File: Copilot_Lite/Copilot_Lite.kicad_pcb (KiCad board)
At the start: 4 copper layers, 65 x 56 mm, 80 parts, among them J1 POWER_MODES, J11 SERIAL_MODE, J12 SERIAL_VOLTAGE_SELECT, J2 JACK_POWER_IN, J3 USB_POWER_IN, J4 USB_PC, J6 5V_ENABLE, J7 SERIAL_AND_GPIO, J8 JACK_POWER_OUT, J9 USB_POWER_OUT, Q1 BSS138, Q2 BUK7M27-80EX, Q3 BUK7M27-80EX, Q4 BSS138, Q5 BSS138, Q6 BSS138, Q7 BSS138, Q8 BSS138, Q9 BSS138, U1 LM74502, U2 LM74502, U3 AP2204K-ADJ, U4 AP2204K-ADJ, U5 FT230XS, U6 SN74LV1T125, U7 SN74LV1T125, U8 SN74LV1T125, U9 SN74LV1T125

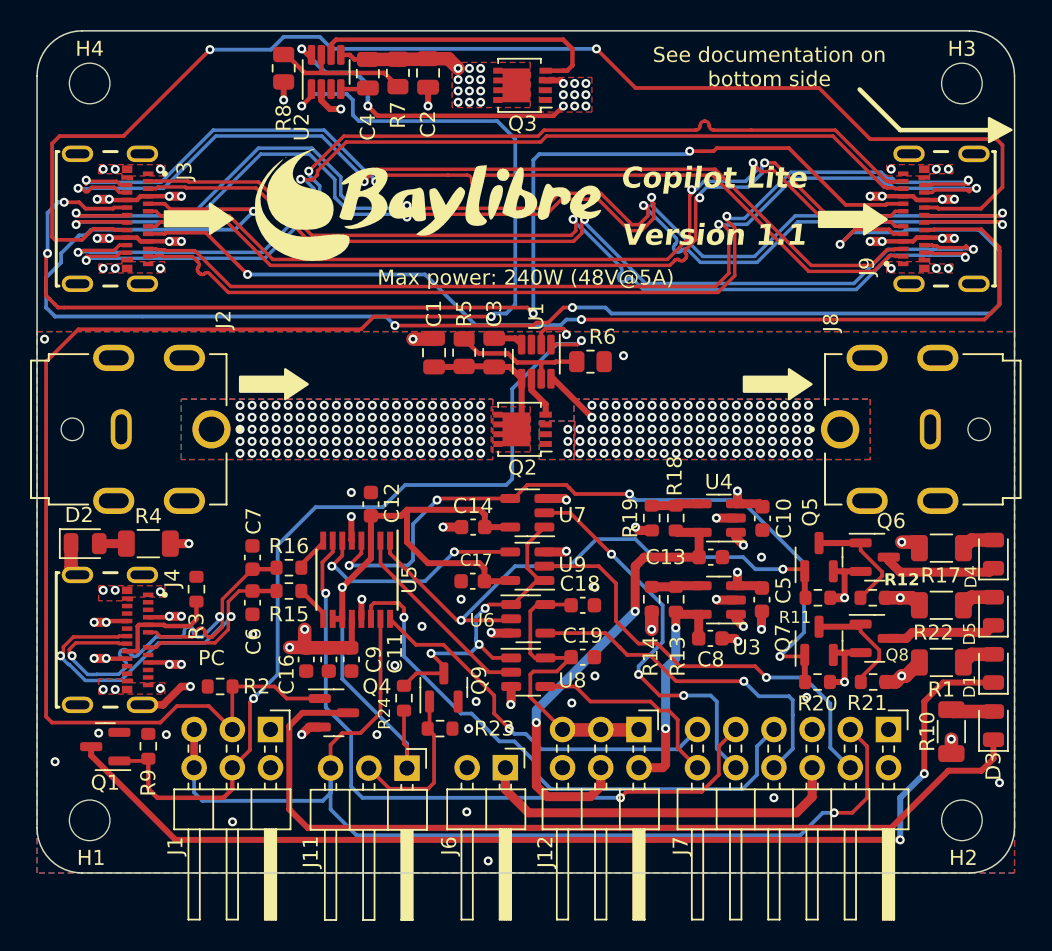
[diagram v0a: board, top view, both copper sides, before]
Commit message: lite: Added even more offset to the USB-C connector shield pins to further improve its centering.
The goal is to make sure all signal pads are well soldered even if the
connector is placed by a human.

Signed-off-by: Adrien Ricciardi <aricciardi@baylibre.com>
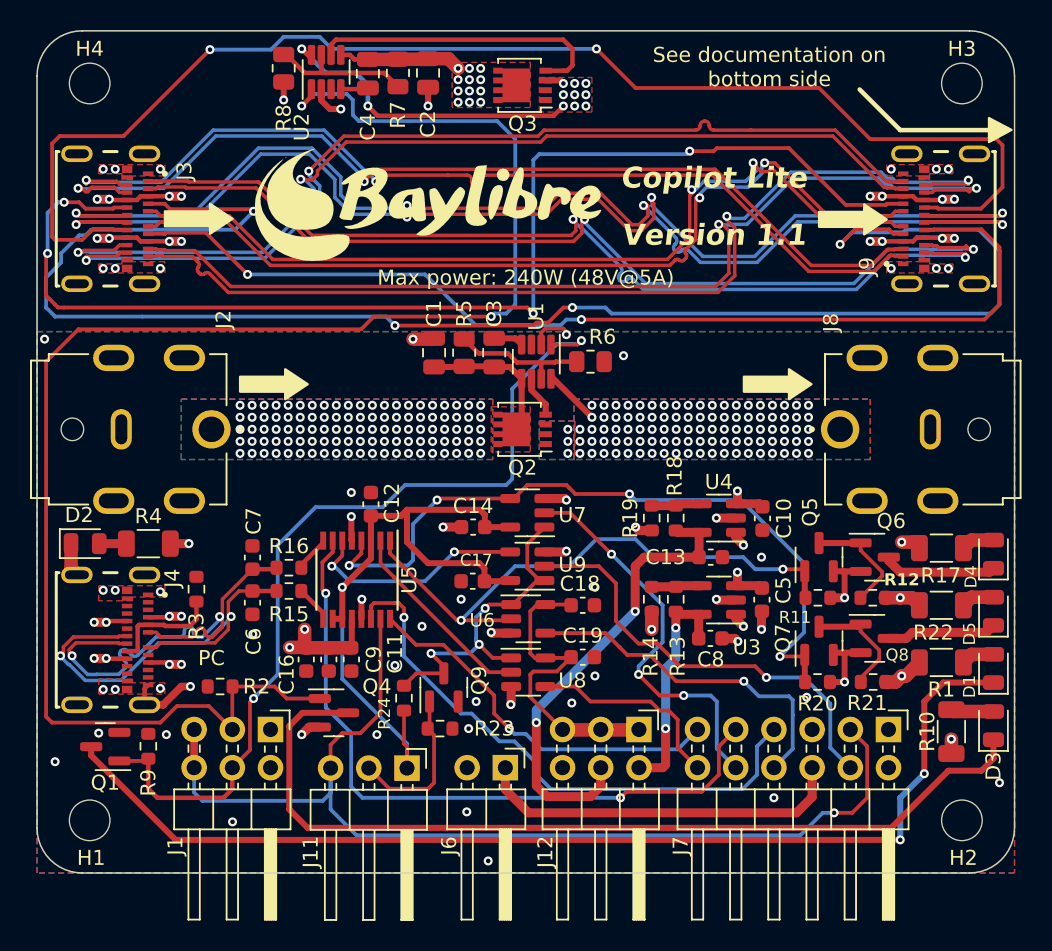
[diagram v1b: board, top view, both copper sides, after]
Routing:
- net GND: track 42.8 -> 44.2 mm
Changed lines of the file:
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@@
     (fp_circle (center -3 -5.05) (end -2.9 -5.05)
       (stroke (width 0.2) (type solid)) (fill none) (layer "F.SilkS"))
-    (fp_line (start -5.12 -4.73) (end -5.12 3.93)
+    (fp_line (start -5.12 -4.8) (end -5.12 3.93)
       (stroke (width 0.05) (type solid)) (layer "F.CrtYd"))
     (fp_line (start -5.12 3.93) (end 5.12 3.93)
       (stroke (width 0.05) (type solid)) (layer "F.CrtYd"))
-    (fp_line (start 5.12 -4.73) (end -5.12 -4.73)
-      (stroke (width 0.05) (type solid)) (layer "F.CrtYd"))
-    (fp_line (start 5.12 3.93) (end 5.12 -4.73)
+    (fp_line (start 5.12 -4.8) (end -5.12 -4.8)
+      (stroke (width 0.05) (type solid)) (layer "F.CrtYd"))
+    (fp_line (start 5.12 3.93) (end 5.12 -4.8)
       (stroke (width 0.05) (type solid)) (layer "F.CrtYd"))
     (fp_line (start -4.47 -4.02) (end 4.47 -4.02)
@@
     (pad "B12" smd rect (at -2.75 -2.54 90) (size 0.3 0.7) (layers "F.Cu" "F.Paste" "F.Mask")
       (net 2 "GND") (pinfunction "GND_B") (pintype "passive"))
-    (pad "S1" thru_hole oval (at -4.322 0.762 90) (size 1.1 2.1) (drill oval 0.6 1.6) (layers "*.Cu" "*.Mask" "F.Paste")
+    (pad "S1" thru_hole oval (at -4.322 0.8 90) (size 1.1 2.1) (drill oval 0.6 1.6) (layers "*.Cu" "*.Mask" "F.Paste")
       (net 2 "GND") (pinfunction "SHIELD") (pintype "passive"))
-    (pad "S2" thru_hole oval (at 4.318 0.762 90) (size 1.1 2.1) (drill oval 0.6 1.6) (layers "*.Cu" "*.Mask" "F.Paste")
+    (pad "S2" thru_hole oval (at 4.318 0.8 90) (size 1.1 2.1) (drill oval 0.6 1.6) (layers "*.Cu" "*.Mask" "F.Paste")
       (net 2 "GND") (pinfunction "SHIELD") (pintype "passive"))
-    (pad "S3" thru_hole oval (at -4.32 -3.556 90) (size 1.1 2.1) (drill oval 0.6 1.6) (layers "*.Cu" "*.Mask" "F.Paste")
+    (pad "S3" thru_hole oval (at -4.32 -3.7 90) (size 1.1 2.1) (drill oval 0.6 1.6) (layers "*.Cu" "*.Mask" "F.Paste")
       (net 2 "GND") (pinfunction "SHIELD") (pintype "passive"))
-    (pad "S4" thru_hole oval (at 4.32 -3.556 90) (size 1.1 2.1) (drill oval 0.6 1.6) (layers "*.Cu" "*.Mask" "F.Paste")
+    (pad "S4" thru_hole oval (at 4.32 -3.7 90) (size 1.1 2.1) (drill oval 0.6 1.6) (layers "*.Cu" "*.Mask" "F.Paste")
       (net 2 "GND") (pinfunction "SHIELD") (pintype "passive"))
     (pad "S5" smd rect (at -3.3 -2.54 90) (size 0.5 0.7) (layers "F.Cu" "F.Paste" "F.Mask")
@@
       (net 2 "GND") (pinfunction "SHIELD") (pintype "passive"))
     (model "${KIPRJMOD}/USB4081.3dshapes/USB4081-03-A.stp"
-      (offset (xyz 0 -3.7 0))
+      (offset (xyz 0 -3.65 0))
       (scale (xyz 1 1 1))
       (rotate (xyz -90 0 0))
@@
     (fp_circle (center -3 -5.05) (end -2.9 -5.05)
       (stroke (width 0.2) (type solid)) (fill none) (layer "F.SilkS"))
-    (fp_line (start -5.12 -4.73) (end -5.12 3.93)
+    (fp_line (start -5.12 -4.8) (end -5.12 3.93)
       (stroke (width 0.05) (type solid)) (layer "F.CrtYd"))
     (fp_line (start -5.12 3.93) (end 5.12 3.93)
       (stroke (width 0.05) (type solid)) (layer "F.CrtYd"))
-    (fp_line (start 5.12 -4.73) (end -5.12 -4.73)
-      (stroke (width 0.05) (type solid)) (layer "F.CrtYd"))
-    (fp_line (start 5.12 3.93) (end 5.12 -4.73)
+    (fp_line (start 5.12 -4.8) (end -5.12 -4.8)
+      (stroke (width 0.05) (type solid)) (layer "F.CrtYd"))
+    (fp_line (start 5.12 3.93) (end 5.12 -4.8)
       (stroke (width 0.05) (type solid)) (layer "F.CrtYd"))
     (fp_line (start -4.47 -4.02) (end 4.47 -4.02)
@@
     (pad "B12" smd rect (at -2.75 -2.54 270) (size 0.3 0.7) (layers "F.Cu" "F.Paste" "F.Mask")
       (net 2 "GND") (pinfunction "GND_B") (pintype "passive"))
-    (pad "S1" thru_hole oval (at -4.322 0.762 270) (size 1.1 2.1) (drill oval 0.6 1.6) (layers "*.Cu" "*.Mask" "F.Paste")
+    (pad "S1" thru_hole oval (at -4.322 0.8 270) (size 1.1 2.1) (drill oval 0.6 1.6) (layers "*.Cu" "*.Mask" "F.Paste")
       (net 2 "GND") (pinfunction "SHIELD") (pintype "passive"))
-    (pad "S2" thru_hole oval (at 4.318 0.762 270) (size 1.1 2.1) (drill oval 0.6 1.6) (layers "*.Cu" "*.Mask" "F.Paste")
+    (pad "S2" thru_hole oval (at 4.318 0.8 270) (size 1.1 2.1) (drill oval 0.6 1.6) (layers "*.Cu" "*.Mask" "F.Paste")
       (net 2 "GND") (pinfunction "SHIELD") (pintype "passive"))
-    (pad "S3" thru_hole oval (at -4.32 -3.556 270) (size 1.1 2.1) (drill oval 0.6 1.6) (layers "*.Cu" "*.Mask" "F.Paste")
+    (pad "S3" thru_hole oval (at -4.32 -3.7 270) (size 1.1 2.1) (drill oval 0.6 1.6) (layers "*.Cu" "*.Mask" "F.Paste")
       (net 2 "GND") (pinfunction "SHIELD") (pintype "passive"))
-    (pad "S4" thru_hole oval (at 4.32 -3.556 270) (size 1.1 2.1) (drill oval 0.6 1.6) (layers "*.Cu" "*.Mask" "F.Paste")
+    (pad "S4" thru_hole oval (at 4.32 -3.7 270) (size 1.1 2.1) (drill oval 0.6 1.6) (layers "*.Cu" "*.Mask" "F.Paste")
       (net 2 "GND") (pinfunction "SHIELD") (pintype "passive"))
     (pad "S5" smd rect (at -3.3 -2.54 270) (size 0.5 0.7) (layers "F.Cu" "F.Paste" "F.Mask")
@@
       (net 2 "GND") (pinfunction "SHIELD") (pintype "passive"))
     (model "${KIPRJMOD}/USB4081.3dshapes/USB4081-03-A.stp"
-      (offset (xyz 0 -3.7 0))
+      (offset (xyz 0 -3.65 0))
       (scale (xyz 1 1 1))
       (rotate (xyz -90 0 0))
@@
     (fp_circle (center -3 -5.05) (end -2.9 -5.05)
       (stroke (width 0.2) (type solid)) (fill none) (layer "F.SilkS"))
-    (fp_line (start -5.12 -4.73) (end -5.12 3.93)
+    (fp_line (start -5.12 -4.8) (end -5.12 3.93)
       (stroke (width 0.05) (type solid)) (layer "F.CrtYd"))
     (fp_line (start -5.12 3.93) (end 5.12 3.93)
       (stroke (width 0.05) (type solid)) (layer "F.CrtYd"))
-    (fp_line (start 5.12 -4.73) (end -5.12 -4.73)
-      (stroke (width 0.05) (type solid)) (layer "F.CrtYd"))
-    (fp_line (start 5.12 3.93) (end 5.12 -4.73)
+    (fp_line (start 5.12 -4.8) (end -5.12 -4.8)
+      (stroke (width 0.05) (type solid)) (layer "F.CrtYd"))
+    (fp_line (start 5.12 3.93) (end 5.12 -4.8)
       (stroke (width 0.05) (type solid)) (layer "F.CrtYd"))
     (fp_line (start -4.47 -4.02) (end 4.47 -4.02)
@@
     (pad "B12" smd rect (at -2.75 -2.54 270) (size 0.3 0.7) (layers "F.Cu" "F.Paste" "F.Mask")
       (net 2 "GND") (pinfunction "GND_B") (pintype "passive"))
-    (pad "S1" thru_hole oval (at -4.322 0.762 270) (size 1.1 2.1) (drill oval 0.6 1.6) (layers "*.Cu" "*.Mask" "F.Paste")
+    (pad "S1" thru_hole oval (at -4.322 0.8 270) (size 1.1 2.1) (drill oval 0.6 1.6) (layers "*.Cu" "*.Mask" "F.Paste")
       (net 2 "GND") (pinfunction "SHIELD") (pintype "passive"))
-    (pad "S2" thru_hole oval (at 4.318 0.762 270) (size 1.1 2.1) (drill oval 0.6 1.6) (layers "*.Cu" "*.Mask" "F.Paste")
+    (pad "S2" thru_hole oval (at 4.318 0.8 270) (size 1.1 2.1) (drill oval 0.6 1.6) (layers "*.Cu" "*.Mask" "F.Paste")
       (net 2 "GND") (pinfunction "SHIELD") (pintype "passive"))
-    (pad "S3" thru_hole oval (at -4.32 -3.556 270) (size 1.1 2.1) (drill oval 0.6 1.6) (layers "*.Cu" "*.Mask" "F.Paste")
+    (pad "S3" thru_hole oval (at -4.32 -3.7 270) (size 1.1 2.1) (drill oval 0.6 1.6) (layers "*.Cu" "*.Mask" "F.Paste")
       (net 2 "GND") (pinfunction "SHIELD") (pintype "passive"))
-    (pad "S4" thru_hole oval (at 4.32 -3.556 270) (size 1.1 2.1) (drill oval 0.6 1.6) (layers "*.Cu" "*.Mask" "F.Paste")
+    (pad "S4" thru_hole oval (at 4.32 -3.7 270) (size 1.1 2.1) (drill oval 0.6 1.6) (layers "*.Cu" "*.Mask" "F.Paste")
       (net 2 "GND") (pinfunction "SHIELD") (pintype "passive"))
     (pad "S5" smd rect (at -3.3 -2.54 270) (size 0.5 0.7) (layers "F.Cu" "F.Paste" "F.Mask")
@@
       (net 2 "GND") (pinfunction "SHIELD") (pintype "passive"))
     (model "${KIPRJMOD}/USB4081.3dshapes/USB4081-03-A.stp"
-      (offset (xyz 0 -3.7 0))
+      (offset (xyz 0 -3.65 0))
       (scale (xyz 1 1 1))
       (rotate (xyz -90 0 0))
@@
   (segment (start 83.8 103.3) (end 83.1 103.3) (width 0.6) (layer "F.Cu") (net 2))
   (segment (start 105.875 95.625) (end 105.875 96.8) (width 0.9) (layer "F.Cu") (net 2))
+  (segment (start 72.15 100.74) (end 72.39 100.5) (width 0.3) (layer "F.Cu") (net 2))
   (segment (start 100 76.8) (end 100.2 77) (width 0.25) (layer "F.Cu") (net 2))
   (segment (start 118.7 94.7) (end 117.75 94.7) (width 0.6) (layer "F.Cu") (net 2))
@@
   (segment (start 118.6 92.9375) (end 119.75 92.9375) (width 0.4) (layer "F.Cu") (net 2))
   (segment (start 118.7 100.3) (end 118.7 98.45) (width 0.4) (layer "F.Cu") (net 2))
+  (segment (start 72.15 101.82) (end 72.15 100.74) (width 0.3) (layer "F.Cu") (net 2))
   (segment (start 98.525 77.8625) (end 98.525 77.075) (width 0.25) (layer "F.Cu") (net 2))
   (segment (start 111.4 97.4) (end 111.6 97.6) (width 0.6) (layer "F.Cu") (net 2))

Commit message: lite: Bumped board version to 1.2.
Signed-off-by: Adrien Ricciardi <aricciardi@baylibre.com>
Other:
- board text added: "Version 1.2"
- board text removed: "Version 1.1"
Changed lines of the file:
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@@
   (title_block
     (title "Copilot Lite")
-    (date "2023-06-28")
-    (rev "1.1")
+    (date "2023-08-25")
+    (rev "1.2")
     (company "(C) BayLibre")
   )
@@
     (effects (font (size 1.4 1.4) (thickness 0.3) bold italic) (justify bottom))
   )
-  (gr_text "Version 1.1" (at 110 71.4) (layer "F.SilkS")
+  (gr_text "Version 1.2" (at 110 71.4) (layer "F.SilkS")
     (effects (font (size 1.4 1.4) (thickness 0.3) bold italic) (justify bottom))
   )
